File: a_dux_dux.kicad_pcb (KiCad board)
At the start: 2 copper layers, 119.8 x 90.9 mm, 24 parts

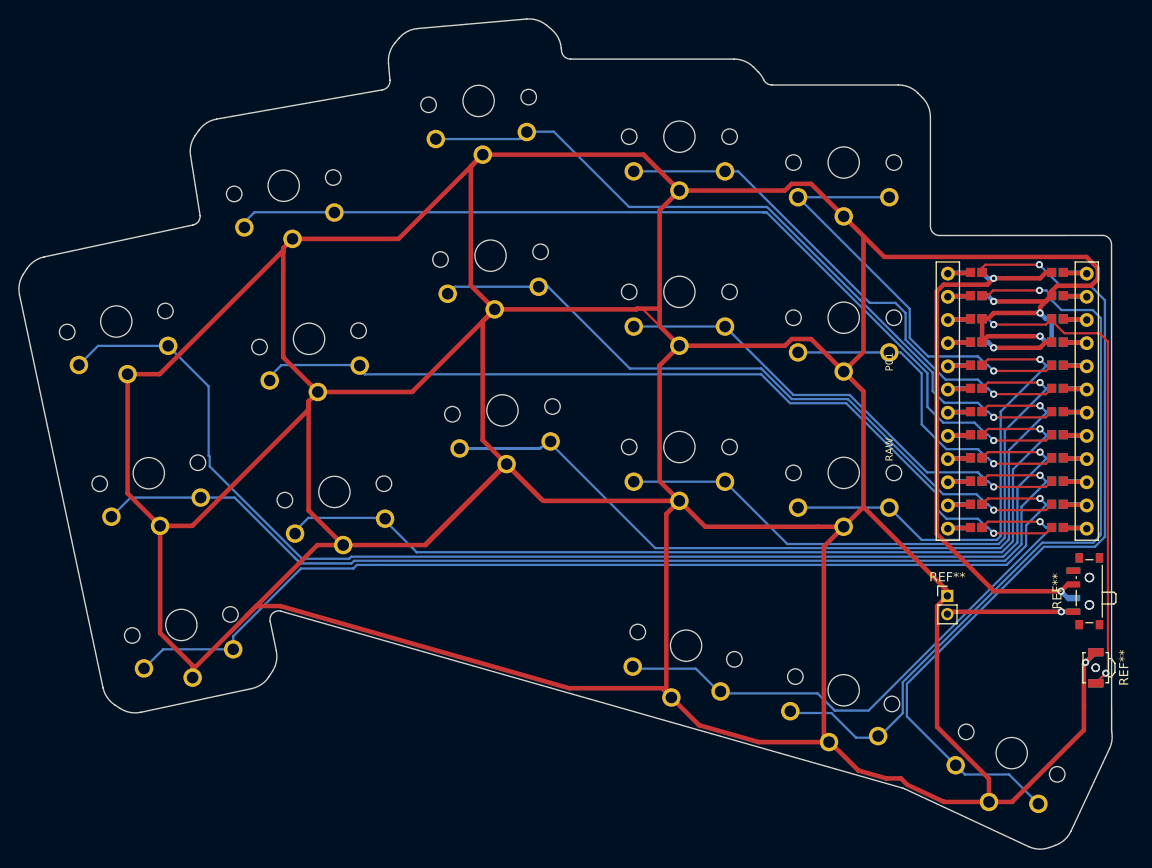
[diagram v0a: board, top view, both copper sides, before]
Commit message: add hotswap support and remove third thumb key
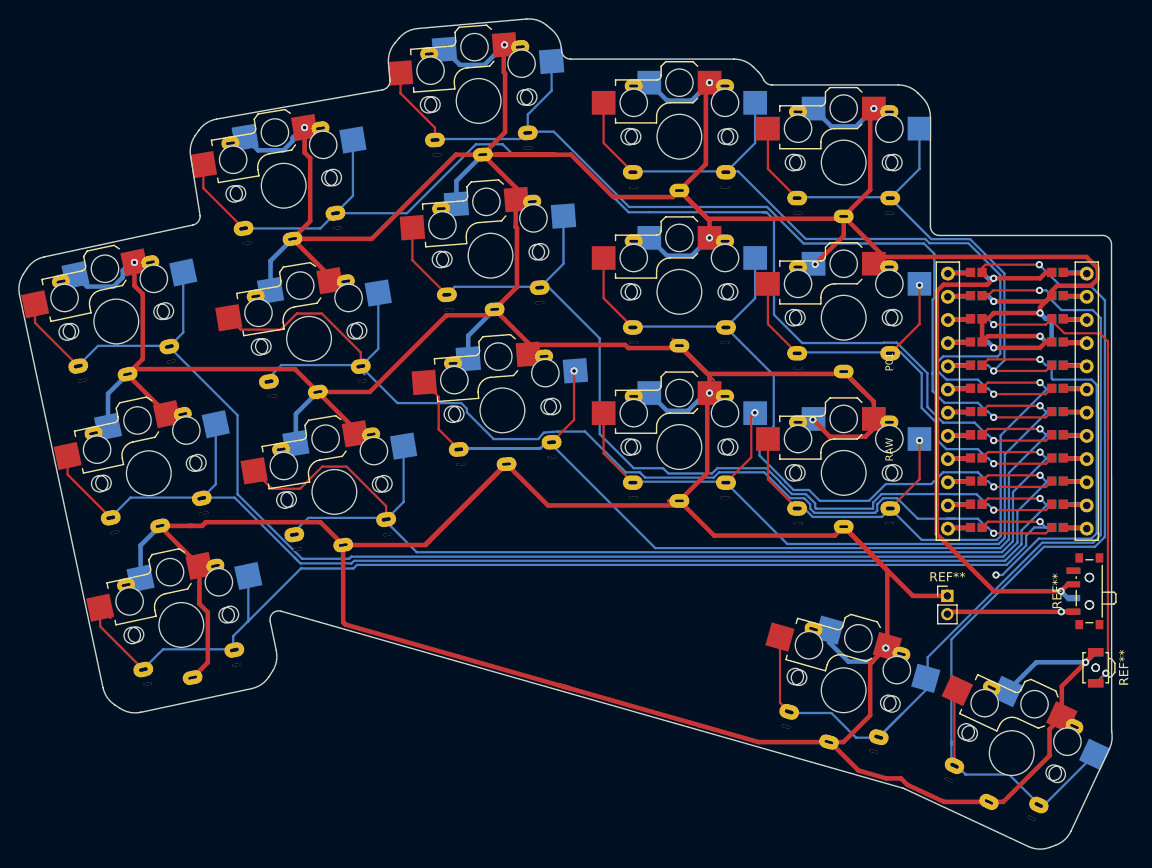
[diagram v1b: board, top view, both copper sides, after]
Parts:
- removed the S32 at (241.6, 161.0)
- removed the S32 at (224.4, 156.1)
- added S32: , depadiernos-parts:CherryMX_ChocV2_1u_flip, F.Cu at (241.6, 161.0)
- S10, S12, S14, S16, S18, S2, S20, S22, S24, S26, S28, S30, S34, S4, S6, S8: footprint PG1350 -> depadiernos-parts:CherryMX_ChocV2_1u_flip
- turned S10 to 9.4 degrees
- turned S12 to 9.4 degrees
- turned S14 to 4.4 degrees
- turned S16 to 4.4 degrees
- turned S18 to 4.4 degrees
- turned S2 to 12.1 degrees
- turned S20 to 0 degrees
- turned S22 to 0 degrees
- turned S24 to 0 degrees
- turned S26 to 0 degrees
- turned S28 to 0 degrees
- turned S30 to 0 degrees
- turned S34 to 335 degrees
- turned S4 to 12.1 degrees
- turned S6 to 12.1 degrees
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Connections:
- S14 pad 1: P4 -> P5
- S2 pad 1: P8 -> P9
- S20 pad 1: P3 -> P4
- S26 pad 1: P2 -> P3
- S4 pad 1: P7 -> P8
- S6 pad 1: P6 -> P7
- S8 pad 1: P5 -> P6
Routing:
- net P9: track 64.3 -> 130.8 mm
- net P20: track 58.2 -> 93.7 mm
- net P7: track 121.6 -> 153.8 mm
- net P10: track 96.0 -> 128.0 mm
- net P18: track 103.2 -> 132.6 mm
- net P14: track 53.6 -> 81.5 mm
- net P16: track 77.7 -> 104.1 mm
- net P19: track 83.2 -> 109.0 mm
- net P8: track 117.2 -> 137.0 mm
- net GND: track 776.8 -> 794.7 mm, vias 4 -> 14
- net P15: track 36.7 -> 54.4 mm, vias 1 -> 2
- net P21: track 48.1 -> 63.1 mm
- net P4: track 99.5 -> 86.0 mm, vias 1 -> 2
- net P1: track 92.2 -> 105.6 mm
- net P0: track 85.0 -> 97.4 mm
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
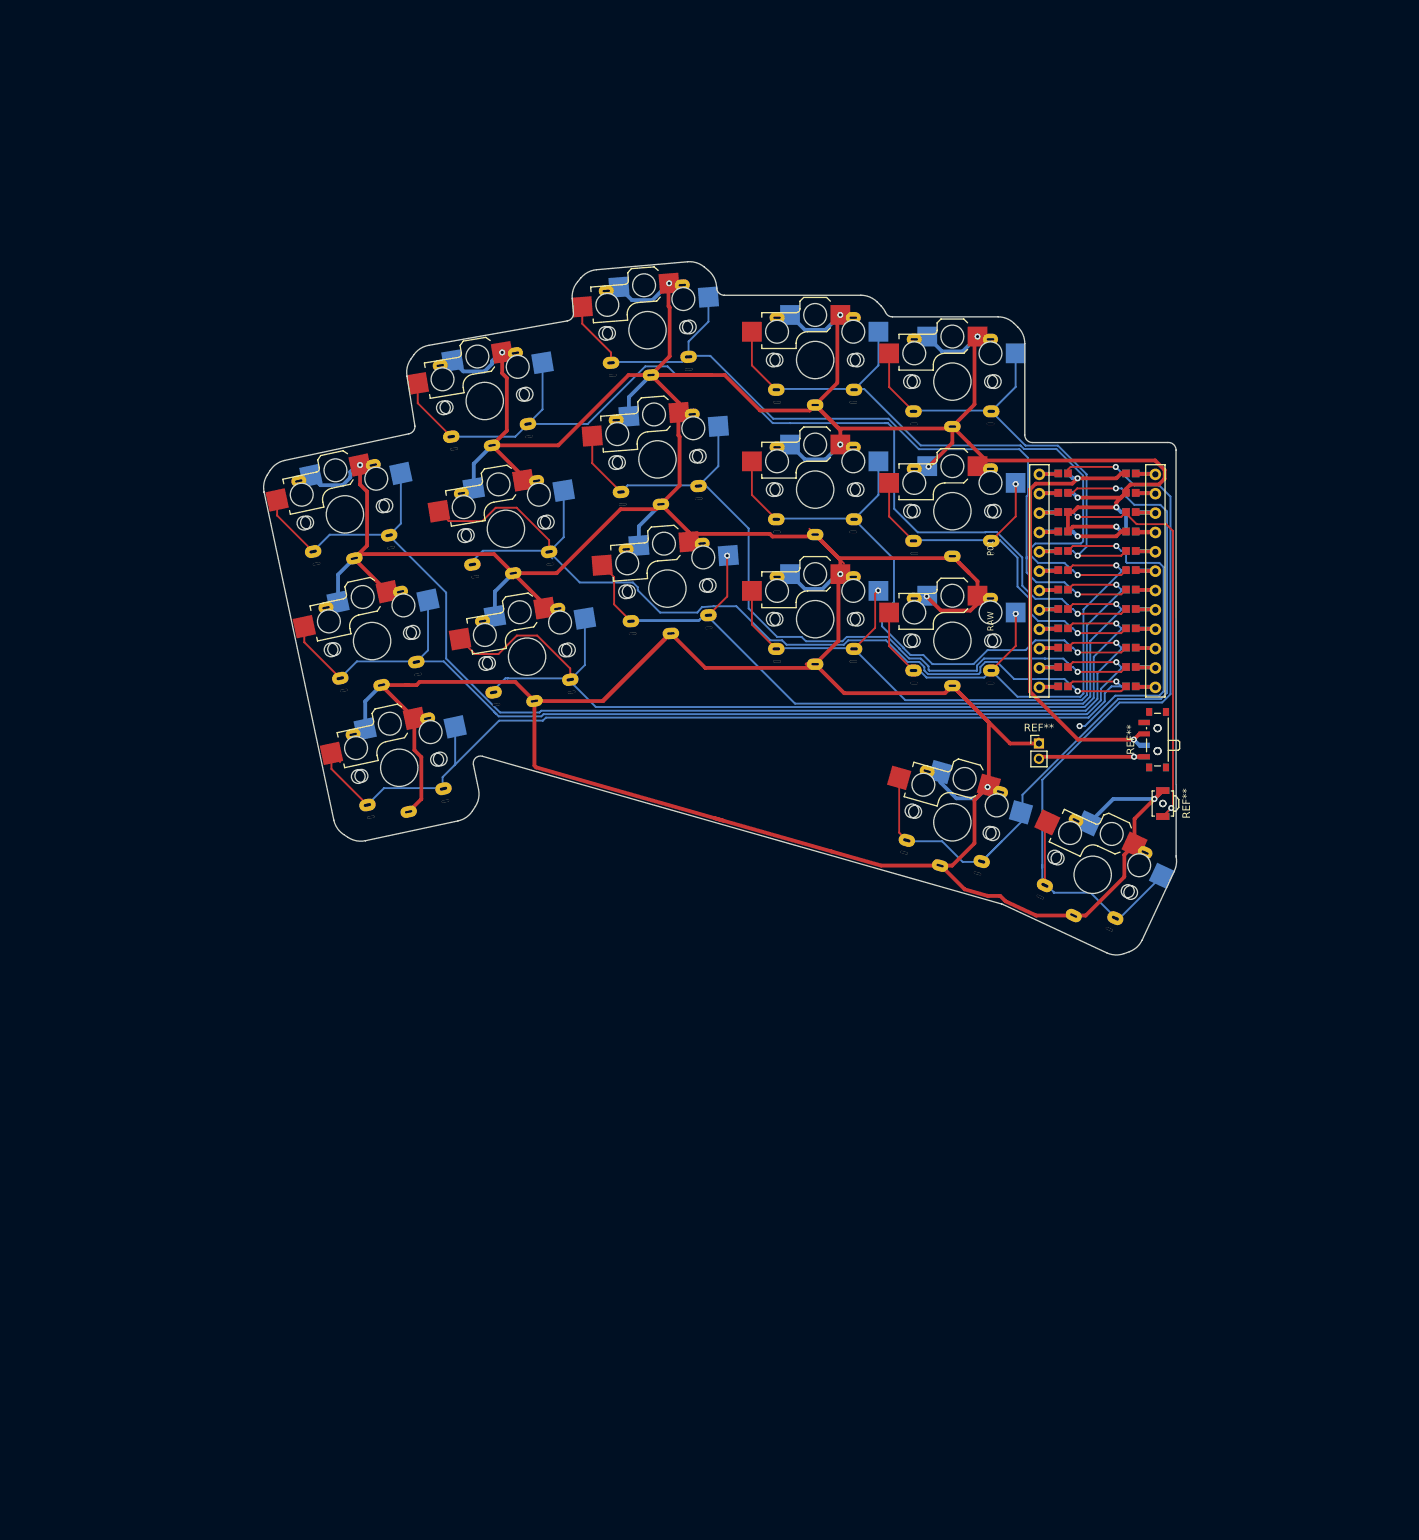
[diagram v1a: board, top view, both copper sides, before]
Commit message: move board to see if that fixes the phantom hole in jlcpcb
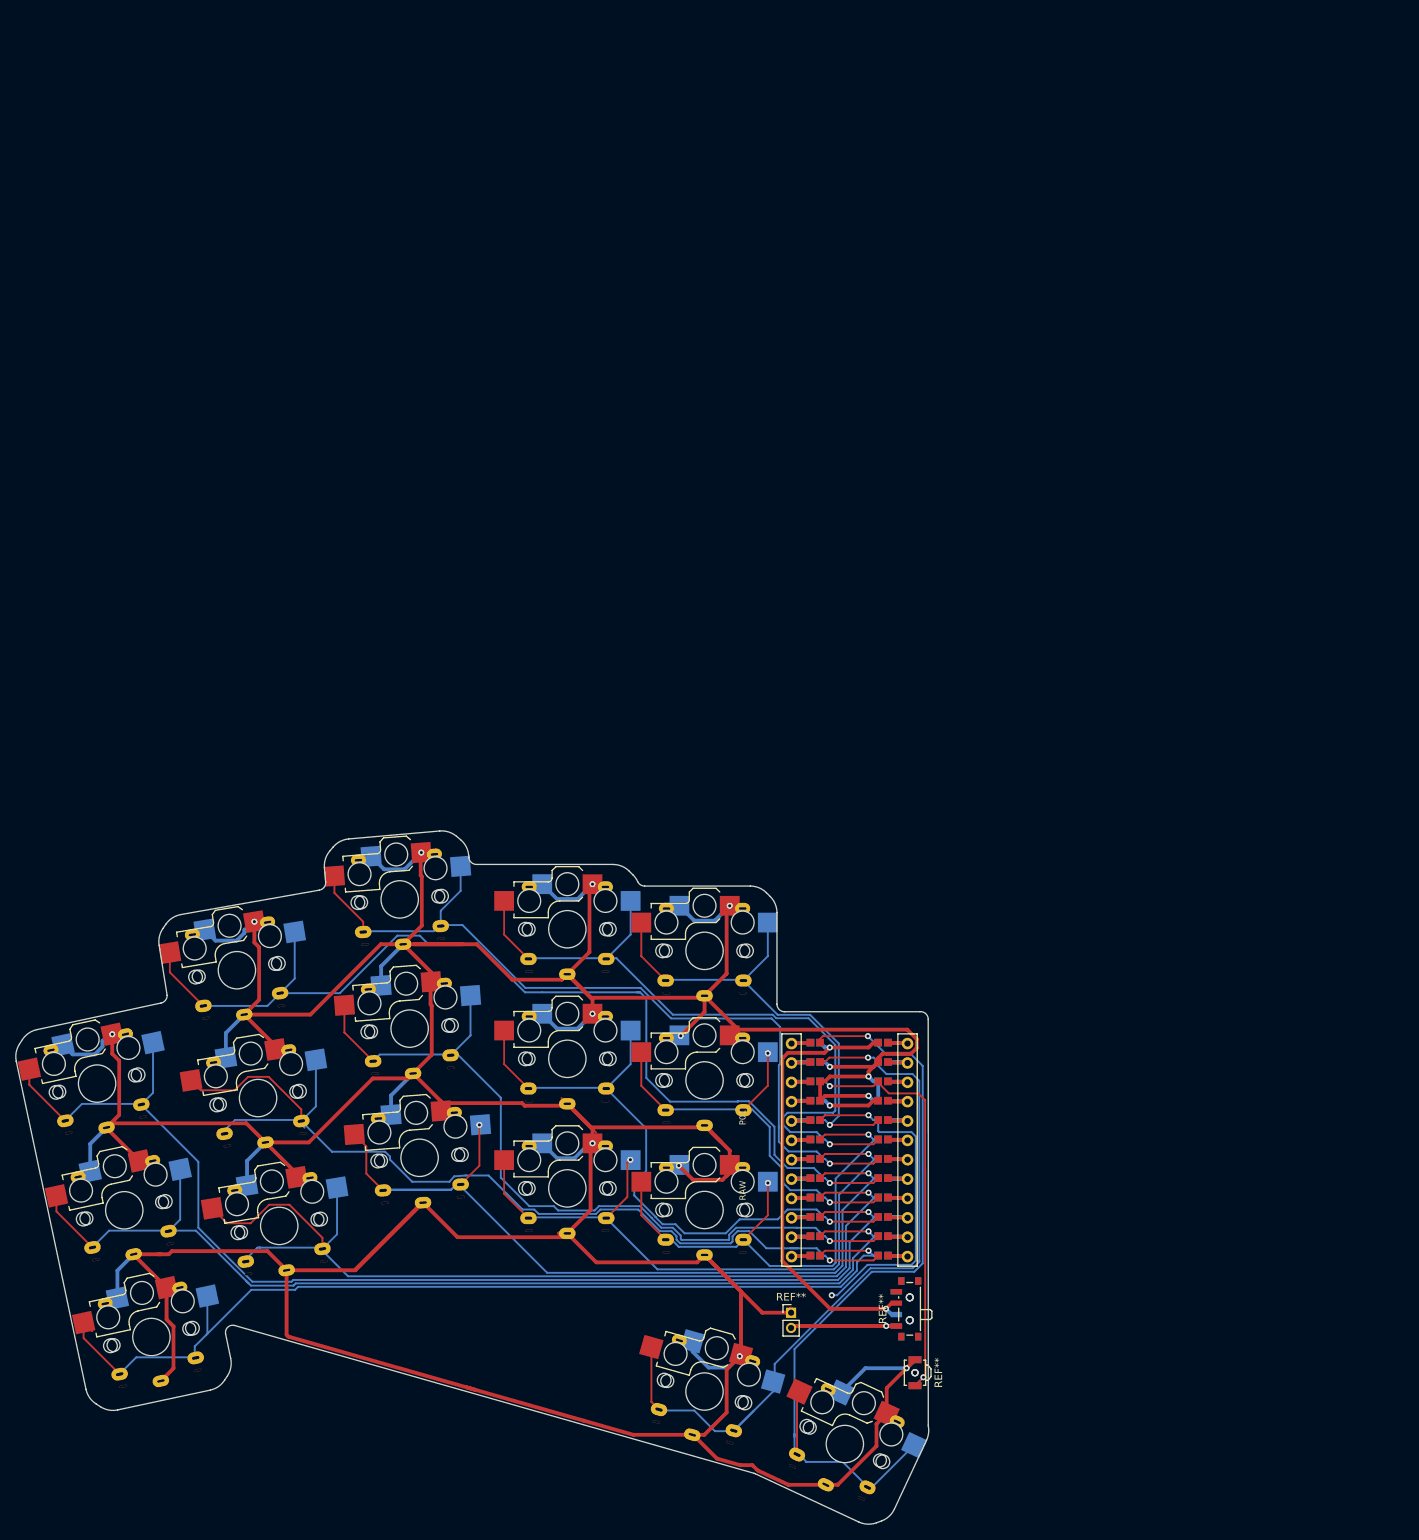
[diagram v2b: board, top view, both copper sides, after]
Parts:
- moved S12 81.4 mm to (147.8, 180.4)
- moved S2 81.4 mm to (136.6, 228.5)
- moved S26 81.4 mm to (209.1, 211.8)
- moved S30 81.4 mm to (209.1, 177.8)
- moved S4 81.4 mm to (133.0, 211.9)
- moved S6 81.4 mm to (129.4, 195.2)
- moved S10 81.4 mm to (150.5, 197.1)
- moved S16 81.4 mm to (170.4, 188.0)
- moved S18 81.4 mm to (169.1, 171.1)
- moved S22 81.4 mm to (191.1, 192.0)
- moved S28 81.4 mm to (209.1, 194.8)
- moved REF** 81.4 mm to (236.7, 233.2)
- moved REF** 81.4 mm to (235.7, 224.8) (x2)
- moved REF** 81.4 mm to (220.5, 225.3)
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
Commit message: update hotswap gerbers
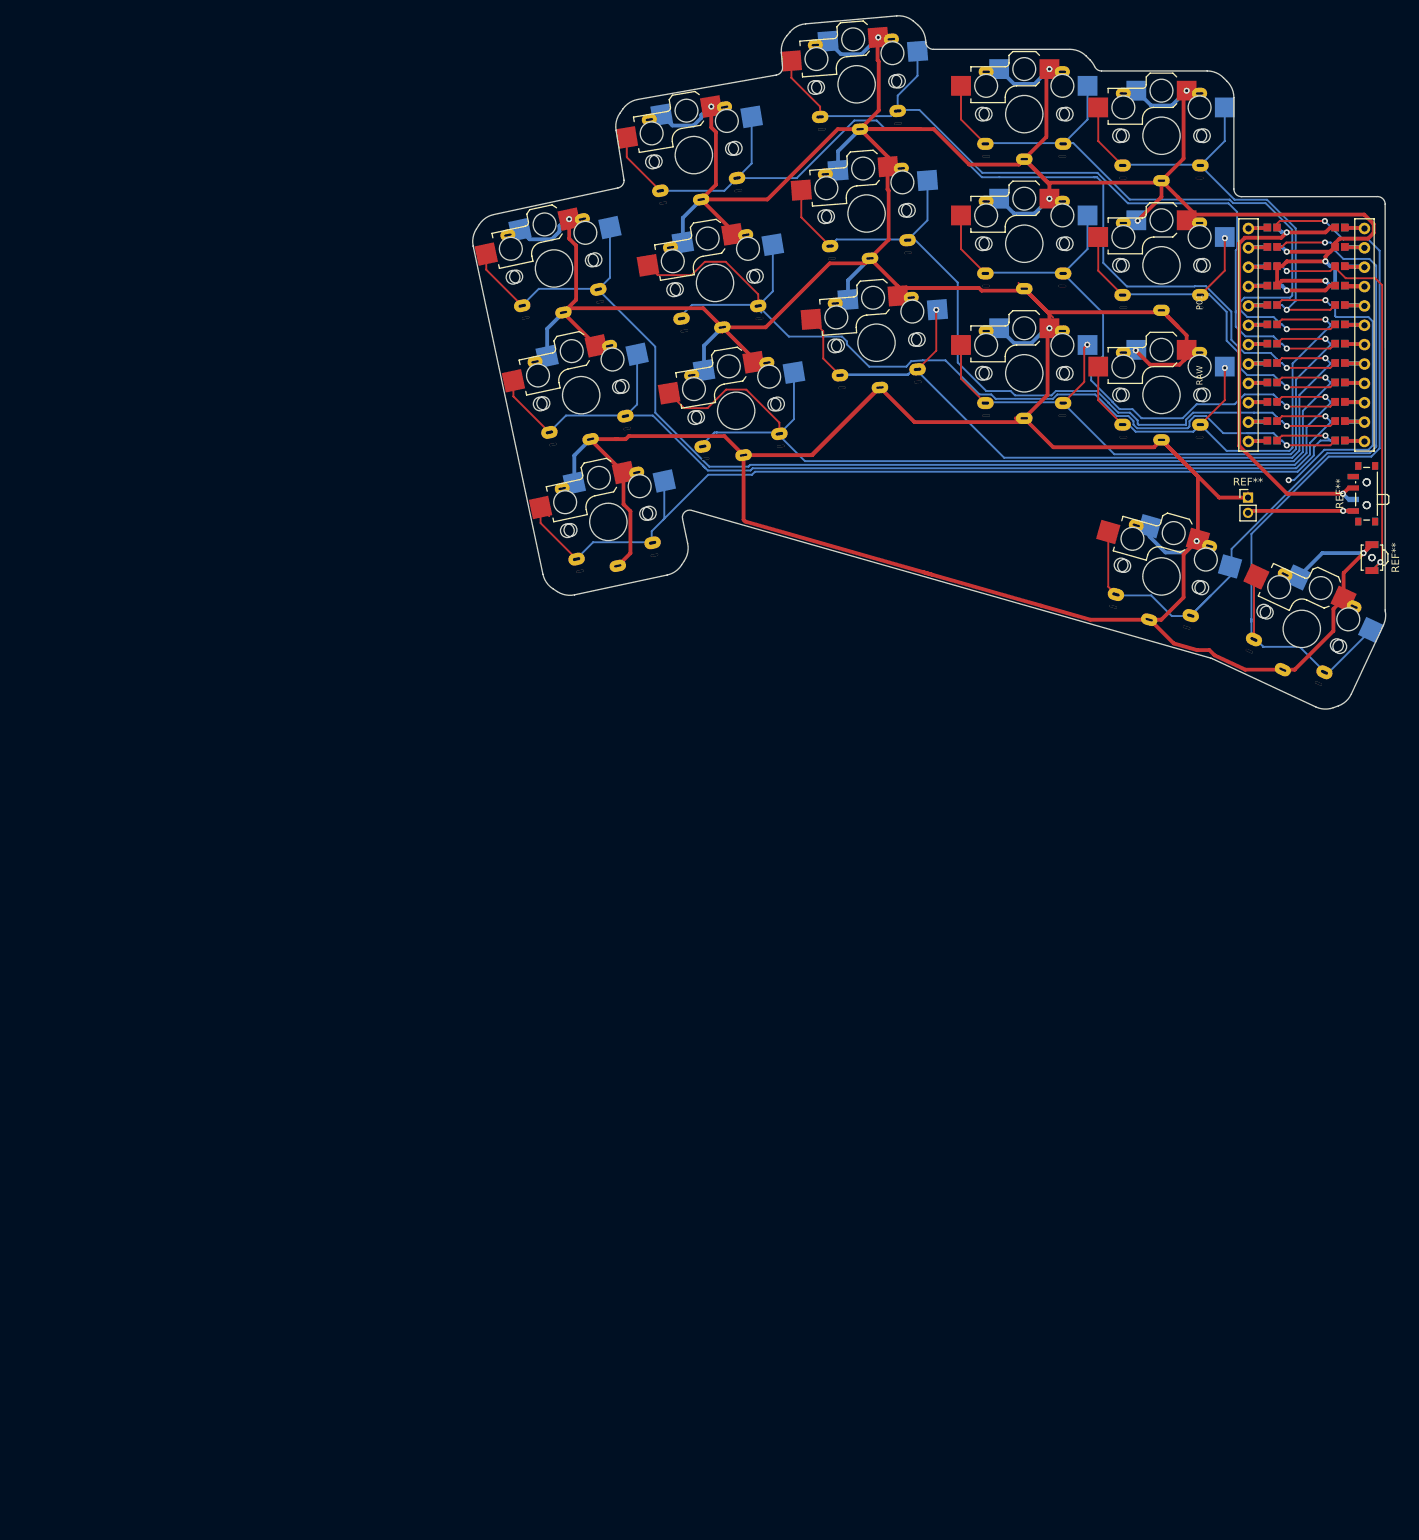
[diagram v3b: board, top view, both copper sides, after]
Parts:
- moved S12 122.6 mm to (207.7, 73.4)
- moved S30 122.6 mm to (269.1, 70.9)
- moved REF** 122.6 mm to (296.7, 126.2) (x2)
- moved REF** 122.6 mm to (295.7, 117.9) (x2)
- moved S14 122.6 mm to (231.7, 98.0)
- moved S16 122.6 mm to (230.4, 81.1)
- moved S32 122.6 mm to (269.1, 128.7)
- moved S34 122.6 mm to (287.5, 135.6)
- moved S18 122.6 mm to (229.1, 64.1)
- moved S22 122.6 mm to (251.1, 85.1)
- moved S6 122.6 mm to (189.4, 88.3)
- moved C1 122.6 mm to (288.0, 97.5)
- moved REF** 122.6 mm to (280.4, 118.4)
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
